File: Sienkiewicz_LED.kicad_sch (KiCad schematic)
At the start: 0 parts

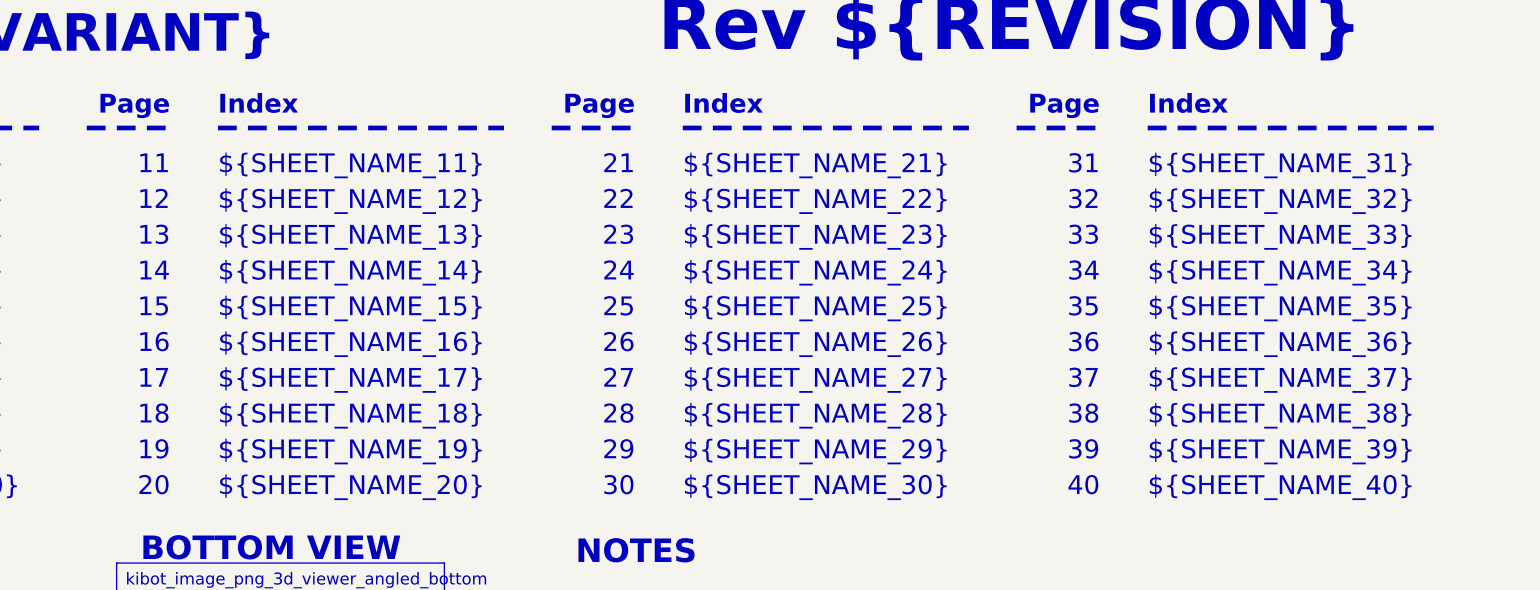
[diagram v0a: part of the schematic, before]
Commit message: documentation update / release 2.1.1 prep
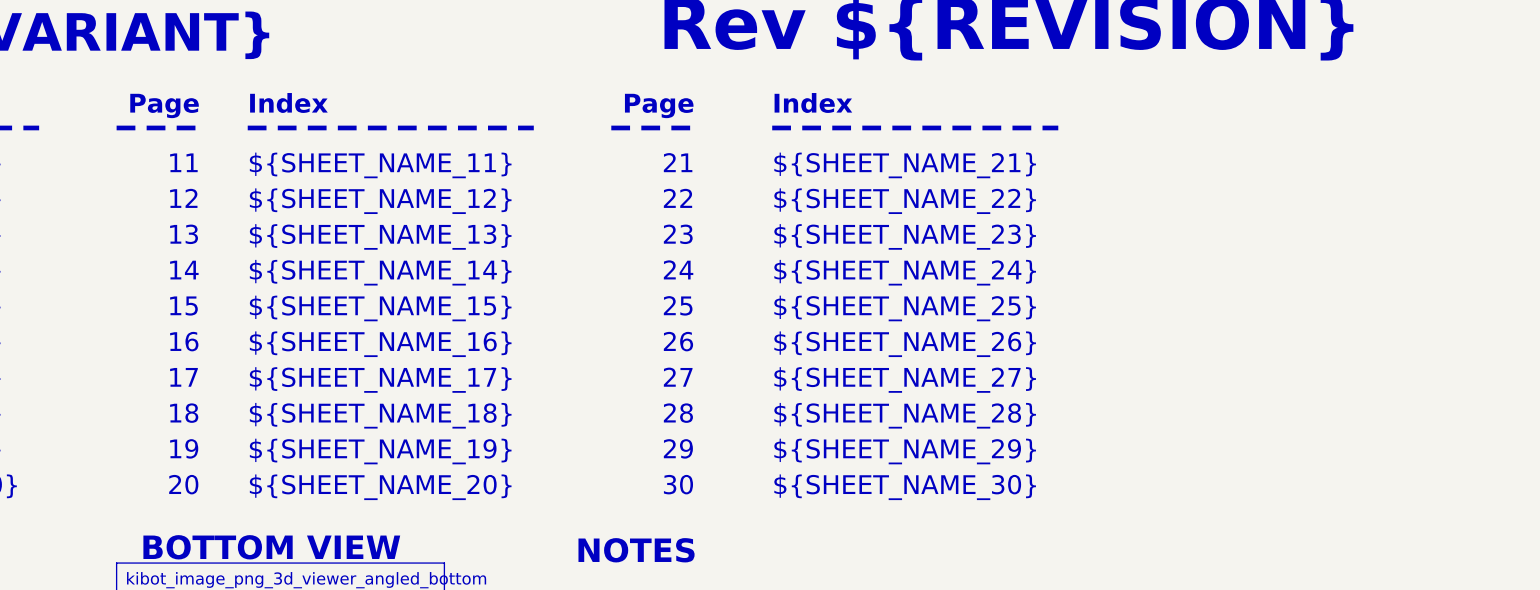
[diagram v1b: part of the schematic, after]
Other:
- note removed: "${SHEET_NAME_31}"
- note removed: "${SHEET_NAME_32}"
- note removed: "${SHEET_NAME_33}"
- note removed: "${SHEET_NAME_34}"
- note removed: "${SHEET_NAME_35}"
- note removed: "${SHEET_NAME_36}"
- note removed: "${SHEET_NAME_37}"
- note removed: "${SHEET_NAME_38}"
- note removed: "${SHEET_NAME_39}"
- note removed: "${SHEET_NAME_40}"
- note removed: "31"
- note removed: "32"
- note removed: "33"
- note removed: "34"
- note removed: "35"
- note removed: "36"
- note removed: "37"
- note removed: "38"
- note removed: "39"
- note removed: "40"
